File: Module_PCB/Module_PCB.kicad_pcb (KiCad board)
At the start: 2 copper layers, 247.5 x 25 mm, 105 parts, among them J1 ISP, J2 US, J3 DS, Q1 HSS2307, Q2 BSS123, U1 W25Q16JV, U2 AP1117-33, U3 TPS563200, U5 ATmega328P-AU, U7 74LVC1G34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

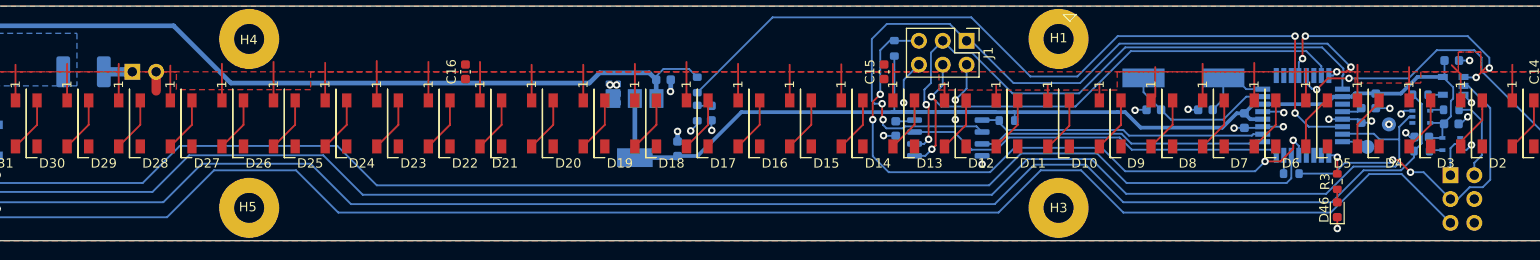
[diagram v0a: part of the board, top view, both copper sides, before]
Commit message: Few smaller fixes in Module_PCB Export of Gerber files, used for first prototype
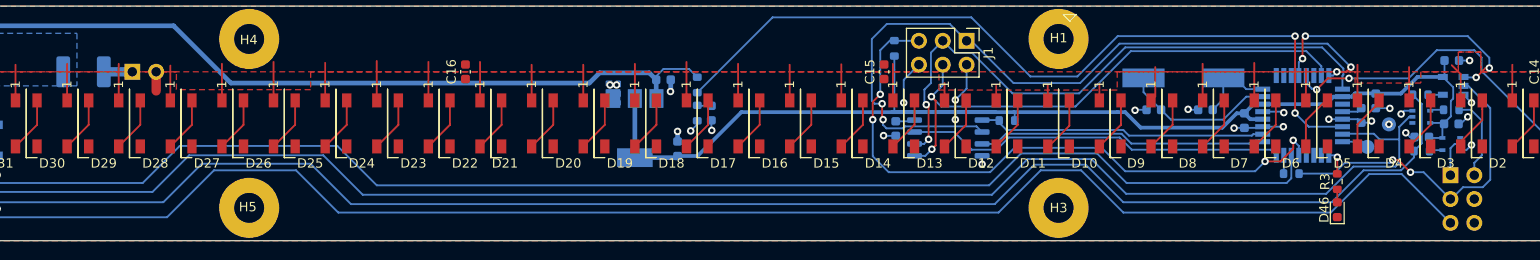
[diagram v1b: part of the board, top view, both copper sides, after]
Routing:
- net GND: track 44.2 -> 43.0 mm, vias 33 -> 32

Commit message: Added copper pour in bottom layer to prevent PCB warping, fixes #11 Moved the large copper pours a bit away from the border to prevent shorts
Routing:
- net /MOSI: track 58.1 -> 57.4 mm
- added copper zone on B.Cu, net +3V3

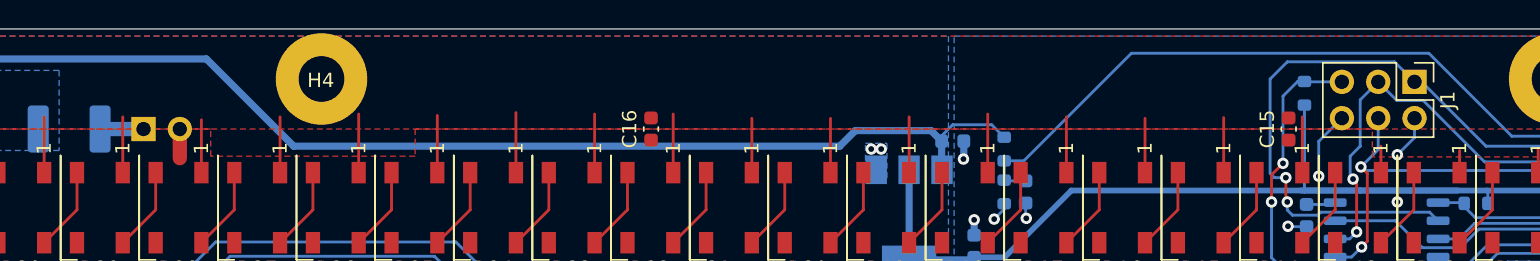
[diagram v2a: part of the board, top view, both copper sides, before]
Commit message: Improved battery connection and added Pin-1 indicator for the ISP header
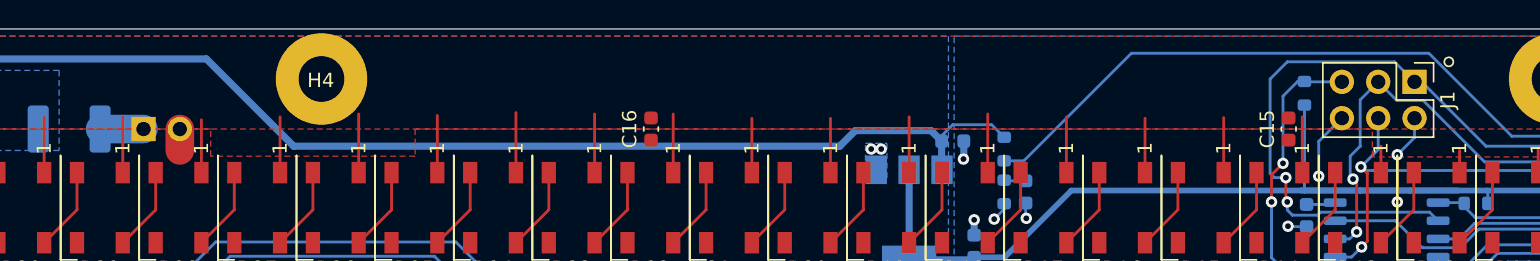
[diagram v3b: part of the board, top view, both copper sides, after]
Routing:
- net GND: track 43.0 -> 42.4 mm

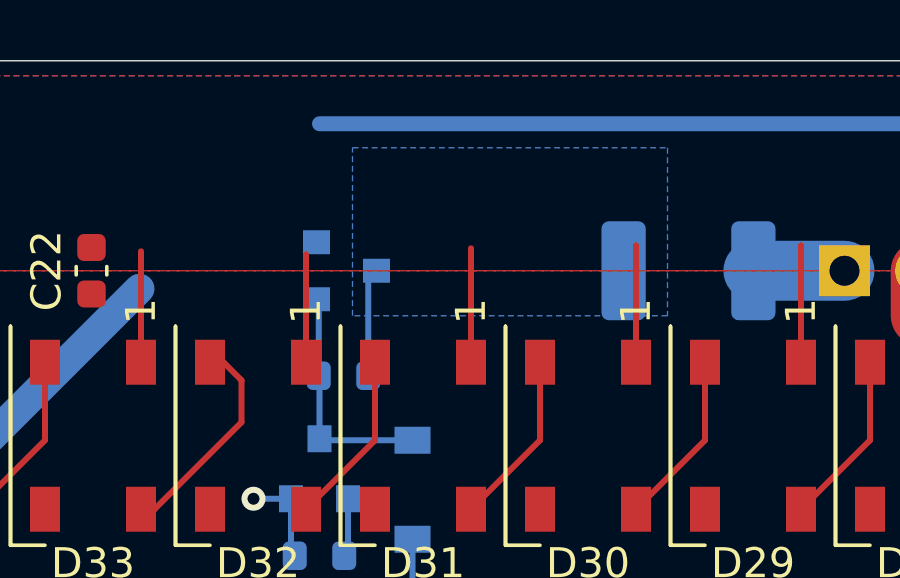
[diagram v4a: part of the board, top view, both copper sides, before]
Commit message: Fixed wrong symbol, wrong pinout, and wrong footprint of p-channel power mosfet
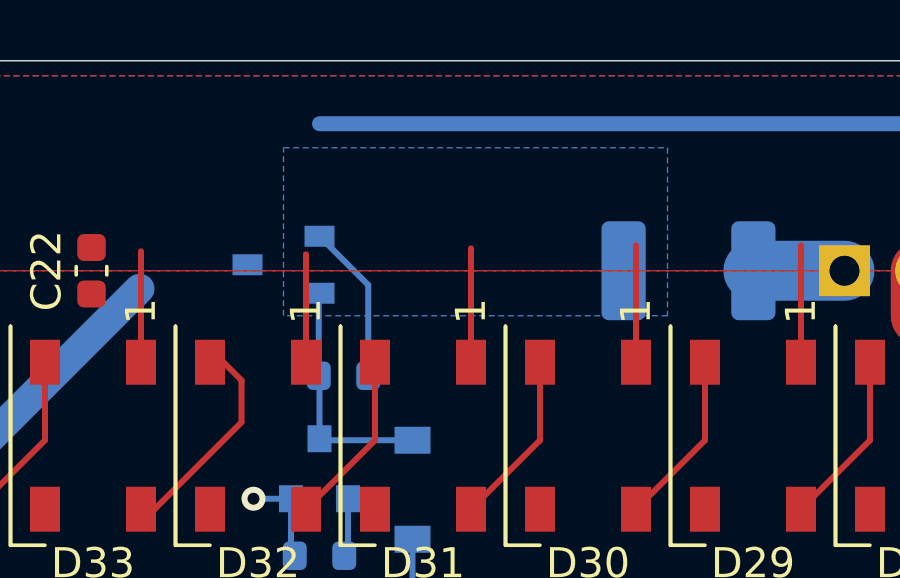
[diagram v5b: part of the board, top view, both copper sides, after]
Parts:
- Q1: value HSS2307 -> Q_PMOS_SGD; footprint Package_TO_SOT_SMD:SOT-23 -> Package_TO_SOT_SMD:SOT-23W
- Y1: value 16MHz -> 8MHz
- moved Q1 2.11 mm to (95.1, 106.8), turned to 180 degrees
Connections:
- Q1 pad 1: Net-(D47-Pad2) -> /BAT_RAW
- Q1 pad 2: +BATT -> Net-(D47-Pad2)
- Q1 pad 3: /BAT_RAW -> +BATT
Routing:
- net /BAT_RAW: track 3.61 -> 5.32 mm

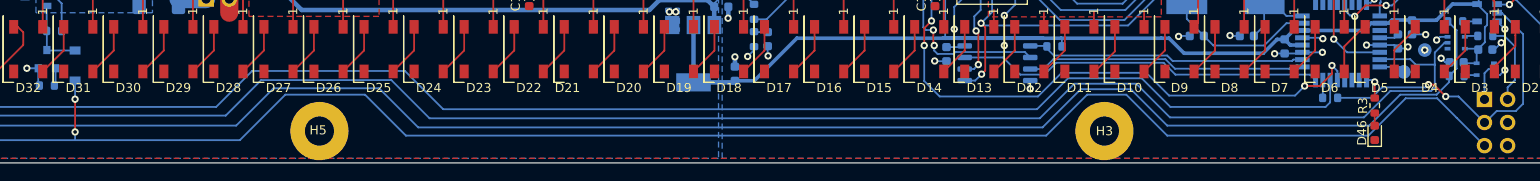
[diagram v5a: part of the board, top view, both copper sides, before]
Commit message: Fixed missing PWR_EN signal
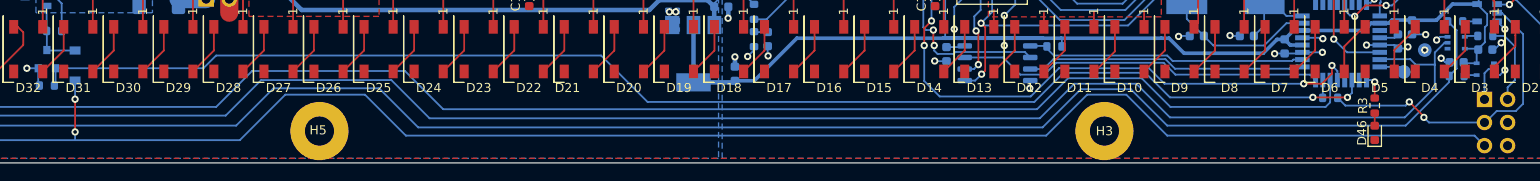
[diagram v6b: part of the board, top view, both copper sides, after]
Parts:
- Q1: value Q_PMOS_SGD -> HSS2307
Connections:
- U5 pad 27: Net-(U5-Pad27) -> /PWR_EN
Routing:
- net /PWR_EN: track 1.95 -> 151.1 mm, vias 0 -> 2
- net /MASTER_ON: track 249.8 -> 246.4 mm
- net /TX: track 35.0 -> 34.2 mm
- net /~RESET: track 67.5 -> 66.9 mm

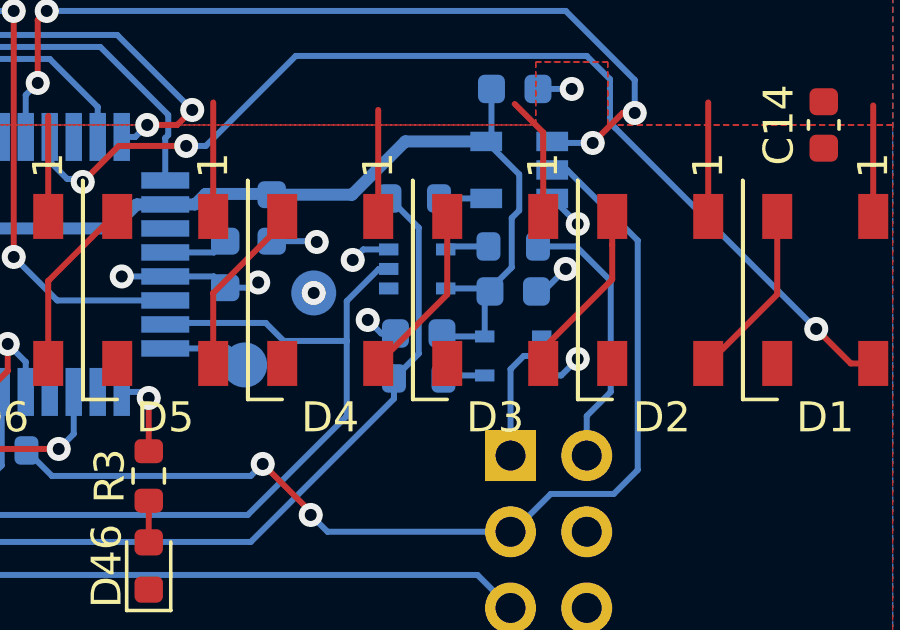
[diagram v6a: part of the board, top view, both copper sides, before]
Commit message: Fixed wrong connection between TX and RETO/RETI
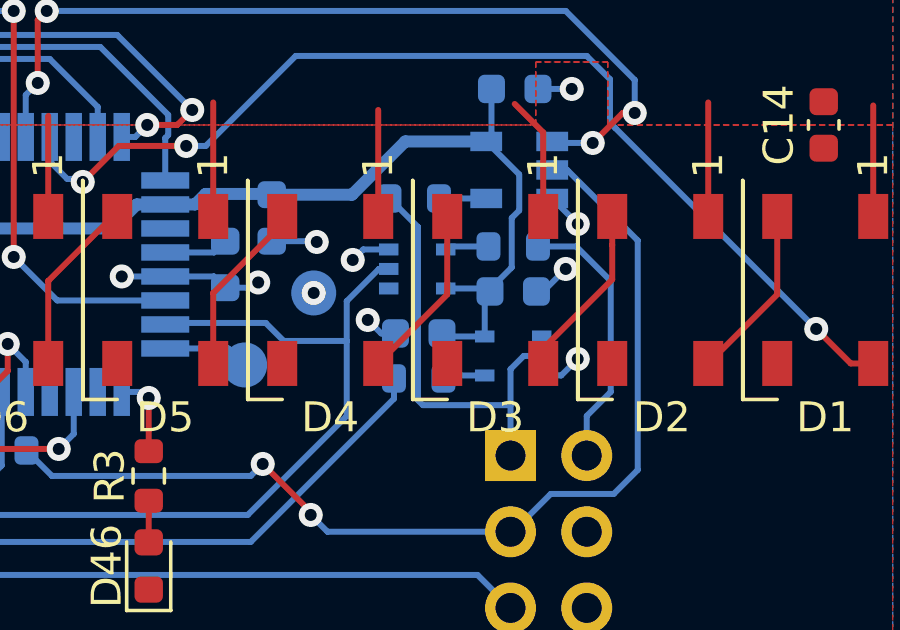
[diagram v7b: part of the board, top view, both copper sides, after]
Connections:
- R12 pad 2: /RETO -> /RETI
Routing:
- net /RETI: track 3.82 -> 14.1 mm
- net /RETO: track 242.2 -> 235.4 mm

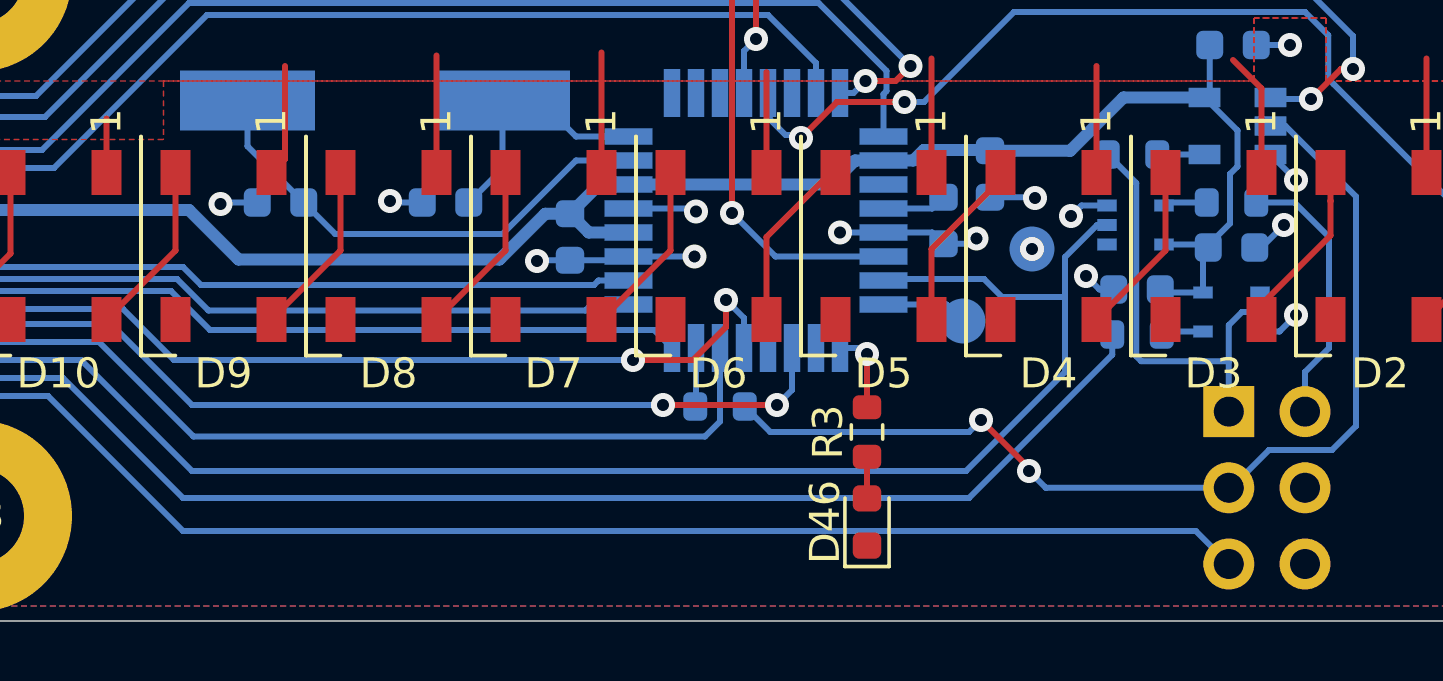
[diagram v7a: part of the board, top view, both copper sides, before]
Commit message: Added pull-up for RETI to ensure high-level uart signal when no module follows and the return path is currently disabled
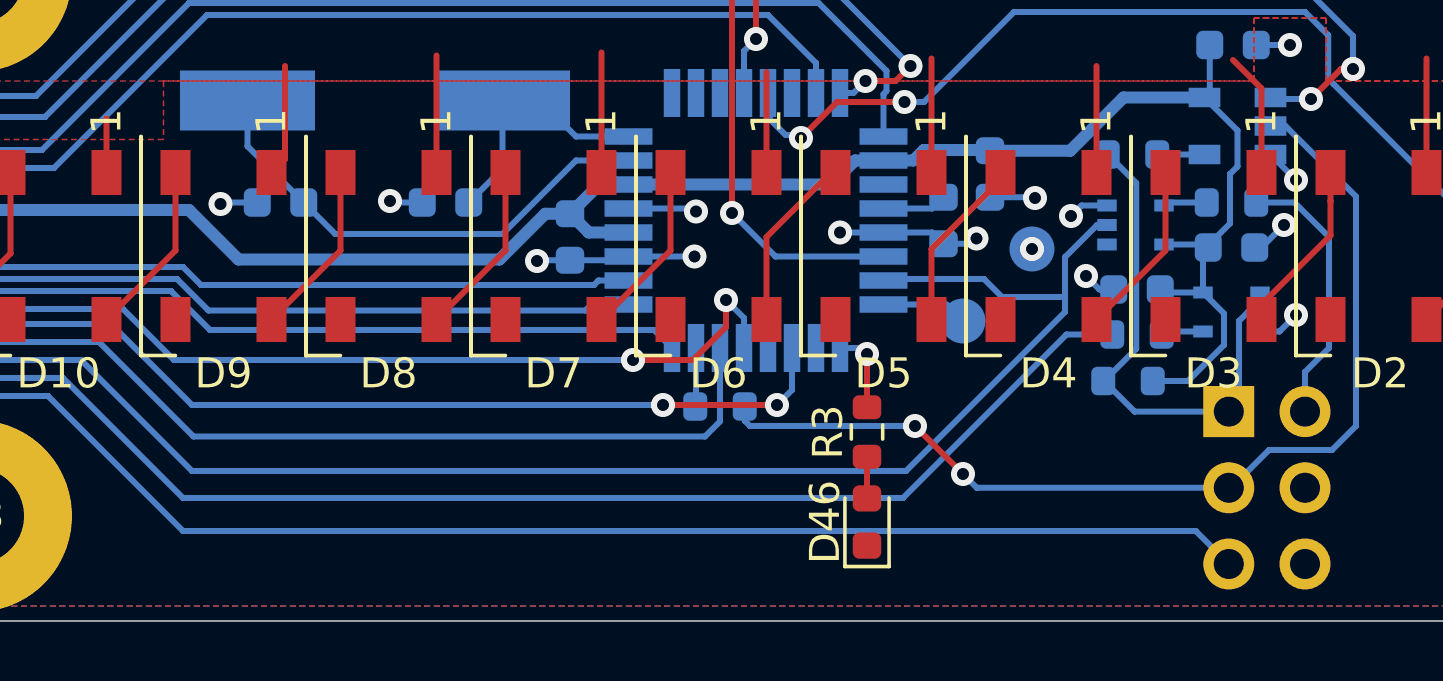
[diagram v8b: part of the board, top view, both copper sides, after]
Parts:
- added R14: 10k, Resistor_SMD:R_0603_1608Metric, B.Cu at (250.9, 117.0)
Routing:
- net +3V3: track 139.8 -> 144.7 mm
- net /RETI: track 14.1 -> 17.5 mm
- net /TRIGI: track 247.2 -> 246.0 mm
